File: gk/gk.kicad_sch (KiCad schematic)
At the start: 62 parts, among them J1 USB_C_Receptacle_USB2.0, J10 Barrel_Jack_Switch, J2 Conn_01x02, J8 Conn_ARM_JTAG_SWD_10, U1 WE-TVS-82400102, U10 MAX17048, U2 MCP73831-2-OT, U3 AP62300WU

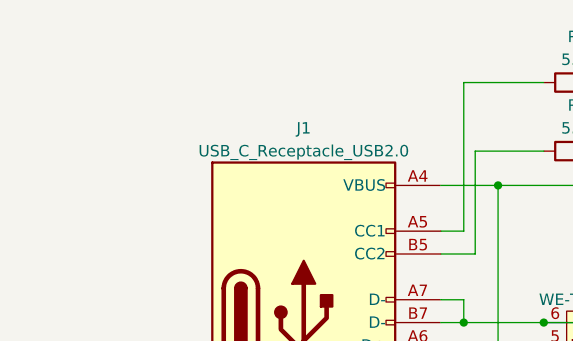
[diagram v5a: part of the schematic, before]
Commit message: Add TODO list to schematic
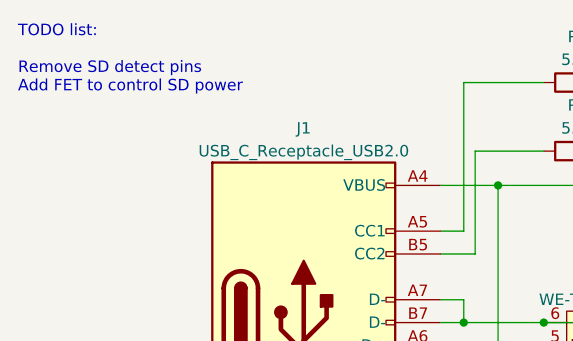
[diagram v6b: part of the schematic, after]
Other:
- note added: "TODO list: Remove SD detect pins Add FET to control SD power"
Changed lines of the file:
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@@
     (stroke (width 0) (type default))
+  )
+  (text "TODO list:\n\nRemove SD detect pins\nAdd FET to control SD power"
+    (at 5.08 22.86 0)
+    (effects (font (size 1.27 1.27)) (justify left bottom))
   )
   (text "VDDA Caps" (at 58.42 148.59 0)

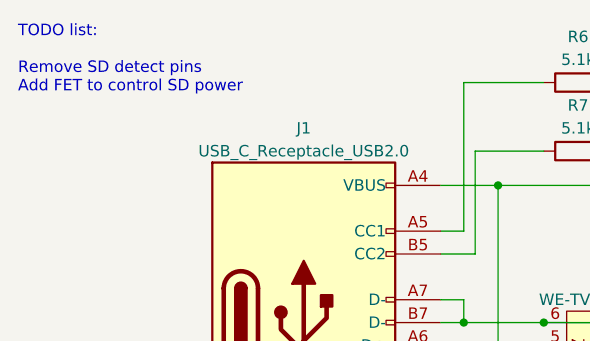
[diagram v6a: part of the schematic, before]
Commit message: Add SD power switch
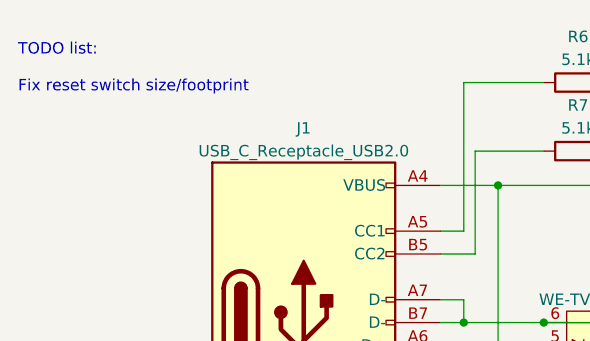
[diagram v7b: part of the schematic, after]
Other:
- note added: "TODO list: Fix reset switch size/footprint"
- note removed: "TODO list: Remove SD detect pins Add FET to control SD power"
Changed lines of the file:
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@@
     (stroke (width 0) (type default))
   )
-  (text "TODO list:\n\nRemove SD detect pins\nAdd FET to control SD power"
-    (at 5.08 22.86 0)
+  (text "TODO list:\n\nFix reset switch size/footprint" (at 5.08 22.86 0)
     (effects (font (size 1.27 1.27)) (justify left bottom))
   )

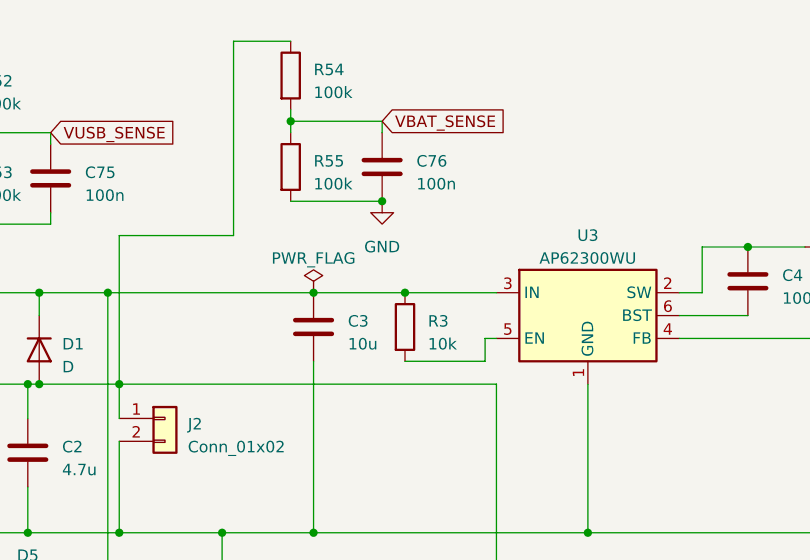
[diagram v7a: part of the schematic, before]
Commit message: update power button routing
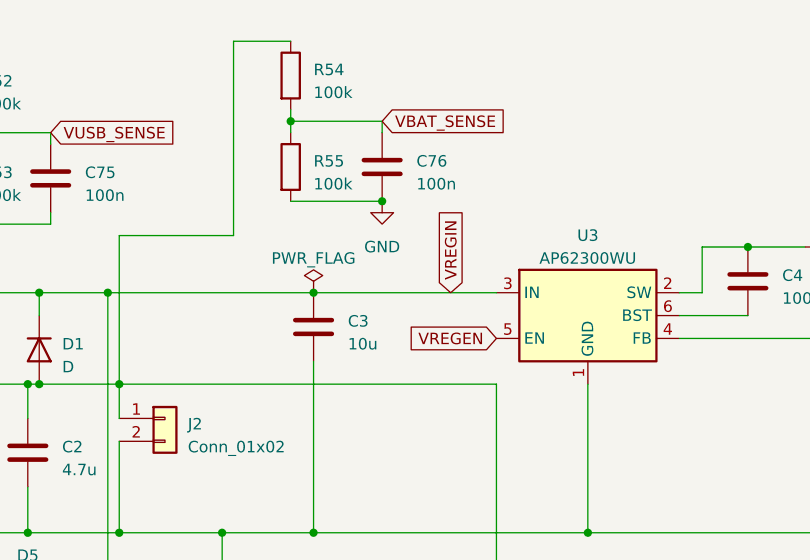
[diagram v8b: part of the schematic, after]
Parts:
- removed R3: 10k, Resistor_SMD:R_0603_1608Metric, symbol Device:R
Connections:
- net VREGIN: now reaches C3.1, D1.1 (K), D2.1 (K), D5.1 (K), U3.3 (IN)
- net VREGEN: now reaches U3.5 (EN)
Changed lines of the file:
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@@
   (junction (at 36.83 72.39) (diameter 0) (color 0 0 0 0)
-  )
-  (junction (at 179.07 45.72) (diameter 0) (color 0 0 0 0)
   )
   (junction (at 151.13 132.08) (diameter 0) (color 0 0 0 0)
@@
     (stroke (width 0) (type default))
   )
-  (wire (pts (xy 187.96 50.8) (xy 189.23 50.8))
-    (stroke (width 0) (type default))
-  )
   (wire (pts (xy 74.93 139.7) (xy 87.63 139.7))
     (stroke (width 0) (type default))
   )
-  (wire (pts (xy 187.96 53.34) (xy 187.96 50.8))
-    (stroke (width 0) (type default))
-  )
   (wire (pts (xy 137.16 55.88) (xy 137.16 59.69))
     (stroke (width 0) (type default))
@@
     (stroke (width 0) (type default))
   )
-  (wire (pts (xy 179.07 45.72) (xy 189.23 45.72))
+  (wire (pts (xy 168.91 45.72) (xy 189.23 45.72))
     (stroke (width 0) (type default))
   )
@@
     (stroke (width 0) (type default))
   )
-  (wire (pts (xy 168.91 45.72) (xy 179.07 45.72))
-    (stroke (width 0) (type default))
-  )
   (wire (pts (xy 93.98 33.02) (xy 81.28 33.02))
     (stroke (width 0) (type default))
@@
   )
   (wire (pts (xy 36.83 132.08) (xy 49.53 132.08))
-    (stroke (width 0) (type default))
-  )
-  (wire (pts (xy 179.07 53.34) (xy 187.96 53.34))
     (stroke (width 0) (type default))
   )
@@
     )
   )
+  (global_label "VREGEN" (shape input) (at 189.23 50.8 180) (fields_autoplaced)
+    (effects (font (size 1.27 1.27)) (justify right))
+    (property "Intersheetrefs" "${INTERSHEET_REFS}" (at 178.9877 50.8 0)
+      (effects (font (size 1.27 1.27)) (justify right) hide)
+    )
+  )
   (global_label "VUSB_SENSE" (shape input) (at 139.7 27.94 0) (fields_autoplaced)
     (effects (font (size 1.27 1.27)) (justify left))
@@
     (effects (font (size 1.27 1.27)) (justify left))
     (property "Intersheetrefs" "${INTERSHEET_REFS}" (at 277.1653 97.79 0)
+      (effects (font (size 1.27 1.27)) (justify left) hide)
+    )
+  )
+  (global_label "VREGIN" (shape input) (at 184.15 45.72 90) (fields_autoplaced)
+    (effects (font (size 1.27 1.27)) (justify left))
+    (property "Intersheetrefs" "${INTERSHEET_REFS}" (at 184.15 36.0219 90)
       (effects (font (size 1.27 1.27)) (justify left) hide)
     )
@@
         )
       )
-    )
-  )
-  (symbol (lib_id "Device:R") (at 179.07 49.53 0) (unit 1)
-    (in_bom yes) (on_board yes) (dnp no) (fields_autoplaced)
-    (property "Reference" "R3" (at 181.61 48.895 0)
-      (effects (font (size 1.27 1.27)) (justify left))
-    )
-    (property "Value" "10k" (at 181.61 51.435 0)
-      (effects (font (size 1.27 1.27)) (justify left))
-    )
-    (property "Footprint" "Resistor_SMD:R_0603_1608Metric" (at 177.292 49.53 90)
-      (effects (font (size 1.27 1.27)) hide)
-    )
-    (property "Datasheet" "~" (at 179.07 49.53 0)
-      (effects (font (size 1.27 1.27)) hide)
-    )
-    (pin "1")
-    (pin "2")
-    (instances
-      (project "gk"
-        (path "/08730ac6-6084-459f-bdf1-86b322355ede"
-          (reference "R3") (unit 1)
-        )
-      )
